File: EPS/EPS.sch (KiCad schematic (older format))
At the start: 2 parts, among them J6 CAN

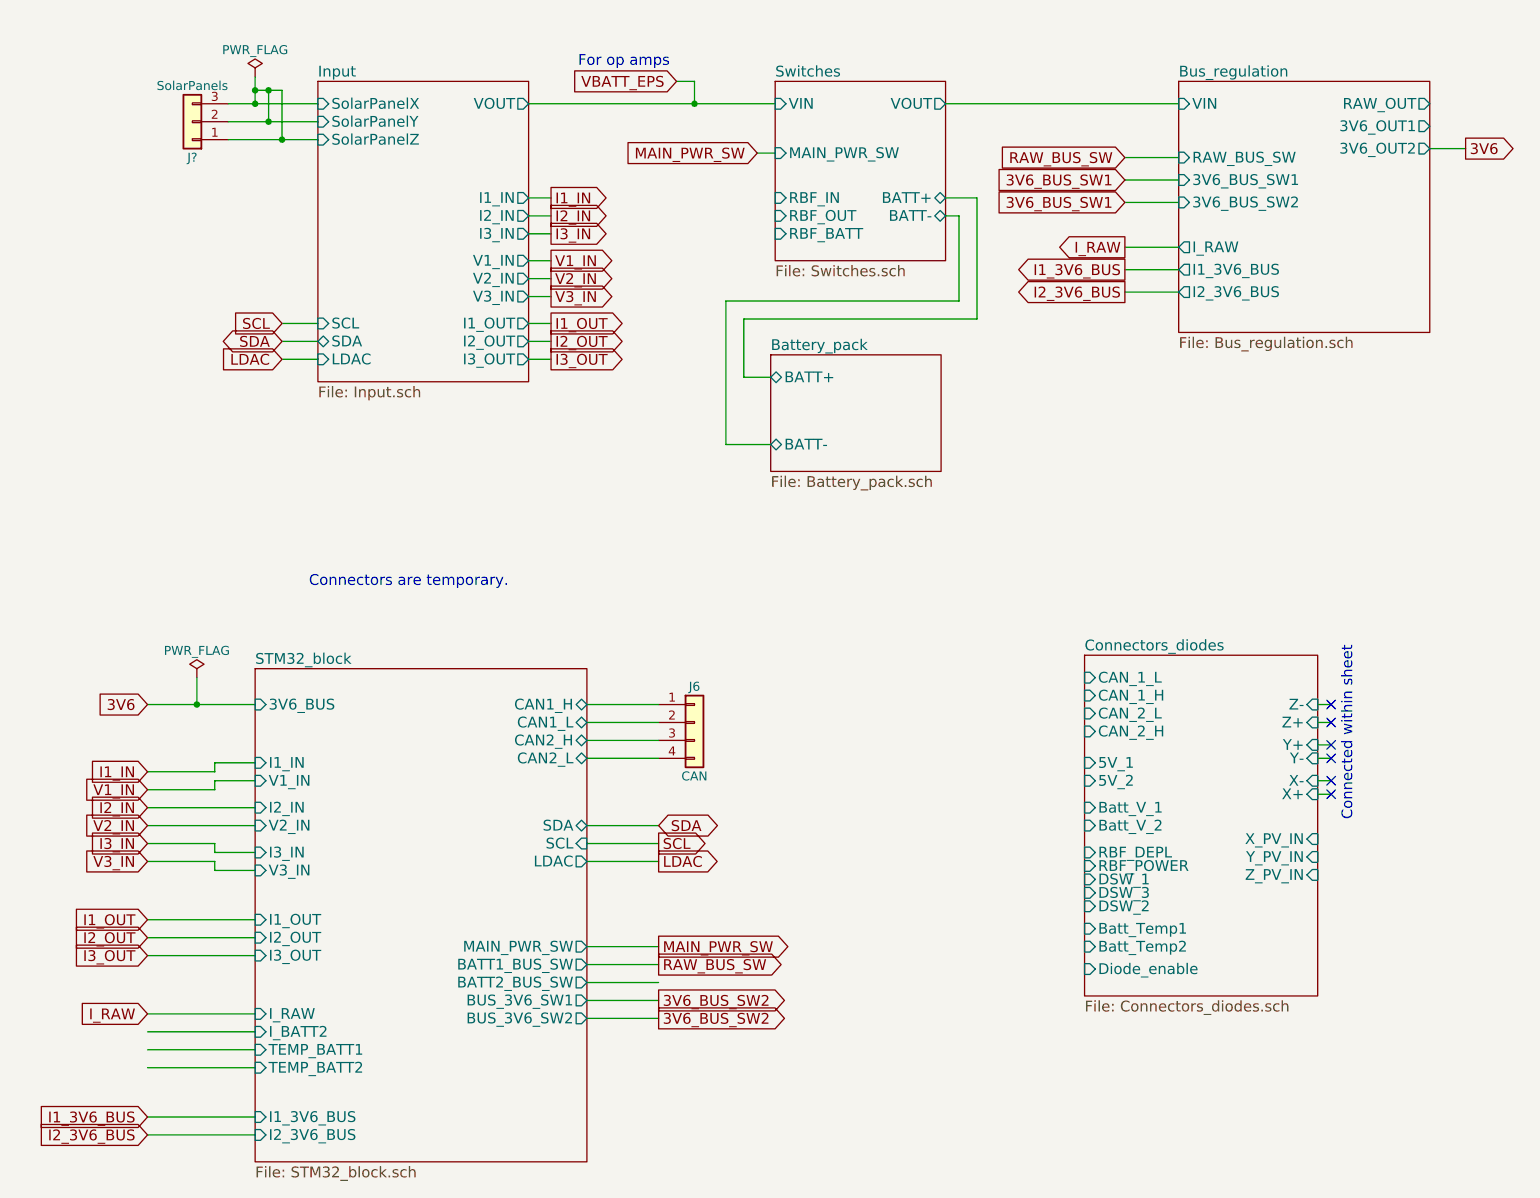
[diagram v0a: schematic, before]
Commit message: Finalized SCH (beta version) and started pcb
Capacitor banks might need to be reassigned to other locations.
No RBF pin on this SCH or PCB.
Battery gound deployment switch is fully mechanical (no mosfet switch on low side).
PCB of the prototype started. Main power converters and current measuring devices layed out.
SCH still requires ESD protection diodes!
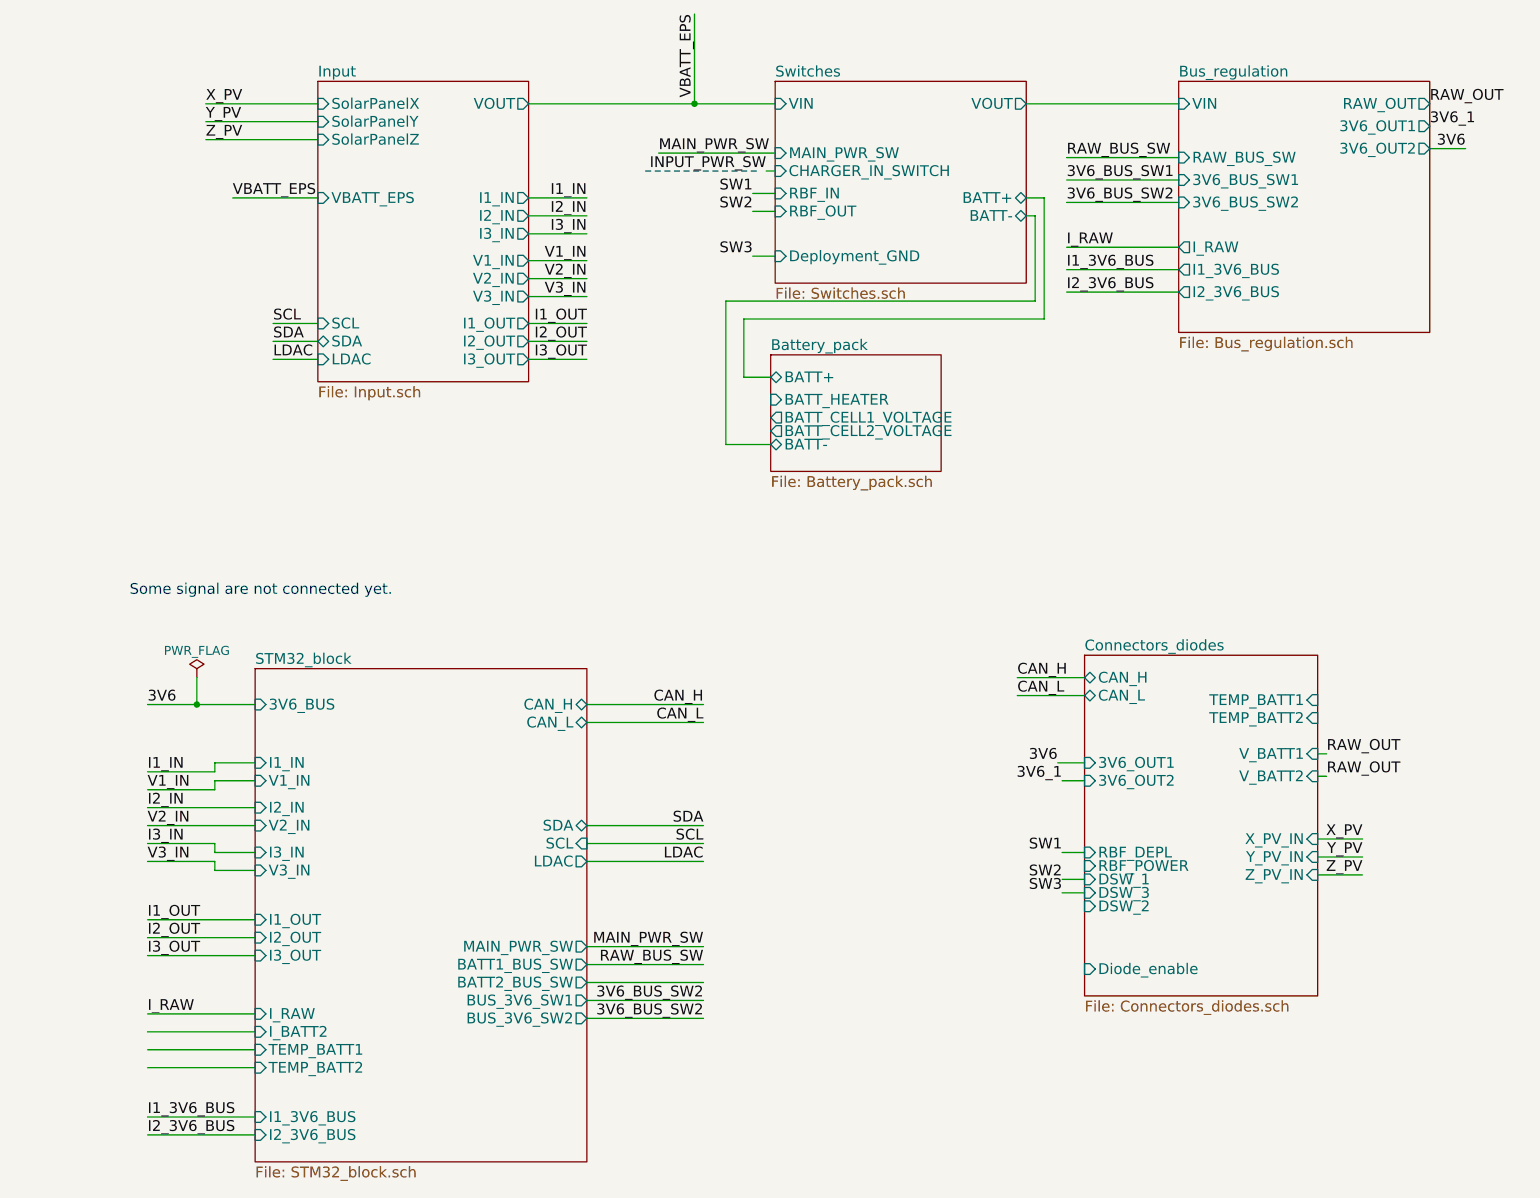
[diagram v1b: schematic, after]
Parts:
- removed J6: CAN, Pin_Headers:Pin_Header_Straight_1x04_Pitch1.00mm, symbol Conn_01x04
- removed J?: SolarPanels, symbol Conn_01x03
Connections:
- net labels added: 3V6_1, CAN_H, CAN_L, INPUT_PWR_SW, RAW_OUT, SW1, SW2, SW3, X_PV, Y_PV, Z_PV
- wire segments 84 -> 88
- no-connect marks 6 -> 0
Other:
- note added: "Some signal are not connected yet."
- note removed: "Connected within sheet\n"
- note removed: "Connectors are temporary."
- note removed: "For op amps"
